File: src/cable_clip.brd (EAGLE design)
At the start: 16.5 x 14 mm, 0 parts

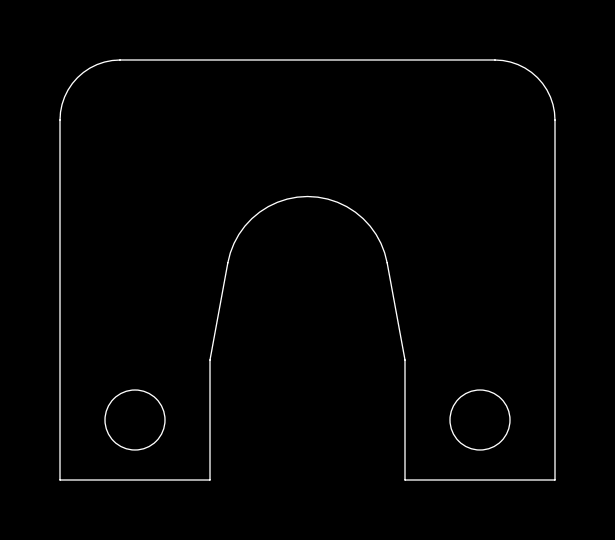
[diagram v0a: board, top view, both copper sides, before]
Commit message: Minor tweaks here and there for better manufacturability
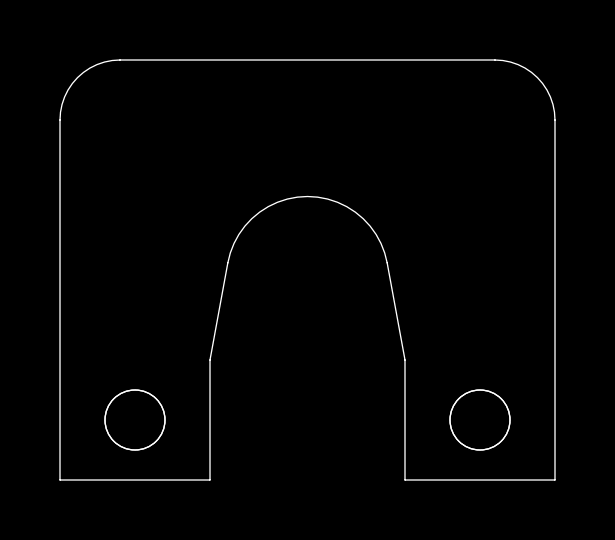
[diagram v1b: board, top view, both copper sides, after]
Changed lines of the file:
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@@
 <setting verticaltext="up"/>
 </settings>
-<grid distance="50" unitdist="mil" unit="mil" style="lines" multiple="1" display="no" altdistance="5" altunitdist="mil" altunit="mil"/>
+<grid distance="0.5" unitdist="mm" unit="mm" style="lines" multiple="1" display="yes" altdistance="5" altunitdist="mil" altunit="mil"/>
 <layers>
 <layer number="1" name="Top" color="4" fill="1" visible="yes" active="yes"/>
@@
 <layer number="43" name="vRestrict" color="2" fill="10" visible="yes" active="yes"/>
 <layer number="44" name="Drills" color="7" fill="1" visible="no" active="yes"/>
-<layer number="45" name="Holes" color="7" fill="1" visible="no" active="yes"/>
+<layer number="45" name="Holes" color="7" fill="1" visible="yes" active="yes"/>
 <layer number="46" name="Milling" color="3" fill="1" visible="no" active="yes"/>
 <layer number="47" name="Measures" color="7" fill="1" visible="no" active="yes"/>
@@
 <wire x1="16.5" y1="12" x2="14.5" y2="14" width="0.000253125" layer="20" curve="90"/>
 <wire x1="2" y1="14" x2="14.5" y2="14" width="0.000253125" layer="20"/>
+<hole x="2.5" y="2" drill="2"/>
+<hole x="14" y="2" drill="2"/>
 </plain>
 <attributes>
